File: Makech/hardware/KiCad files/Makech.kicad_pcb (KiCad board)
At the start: 2 copper layers, 54.9 x 88.5 mm, 50 parts, among them IC1 ULN2803, J1 SWD programmer, J2 USB_B_Micro, J3 ESP32-Exp, SW1 RST, SW2 SW_DPDT_x2, U1 ATSAMD21G18A-AU, U2 CONN_01X04, U3 AP2114_3.3v, X1 Screw_Terminal_1x02

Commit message: PCB COMPLETE
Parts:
- moved G*** 13.1 mm to (106.3, 90.9)
- moved SW1 1.24 mm to (128.5, 88.4)
- moved C2 0.79 mm to (132.6, 82.8)
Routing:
- net +3V3: track 31.9 -> 115.4 mm, vias 1 -> 6
- net Net-(R4-Pad2): track 12.5 -> 90.6 mm, vias 0 -> 2
- net /A1: track 0.00 -> 72.7 mm, vias 0 -> 6
- net /A2: track 0.00 -> 63.5 mm, vias 0 -> 6
- net Net-(SW1-Pad2): track 0.00 -> 63.5 mm, vias 0 -> 4
- net /SDA: track 0.00 -> 59.2 mm, vias 0 -> 1
- net /A0: track 0.00 -> 52.6 mm, vias 0 -> 6
- net /A6: track 2.54 -> 50.0 mm, vias 0 -> 4
- net Net-(R6-Pad2): track 12.5 -> 44.0 mm
- net +6V: track 76.4 -> 91.7 mm
- net Net-(F1-Pad1): track 17.5 -> 19.8 mm
- net /D7: track 35.4 -> 37.2 mm
- net /A3: track 45.0 -> 43.3 mm
- net /D4: track 17.3 -> 18.7 mm
- net /SCL: track 62.3 -> 61.0 mm
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
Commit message: v0.1
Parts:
- moved SW2 0.85 mm to (101.2, 89.1)
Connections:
- J3 pad 11: /ESP_RESET -> GND
- J3 pad 3: /ESP_CS -> +3V3
- U1 pad 23: /ESP_CS -> +3V3
- U1 pad 32: /ESP_RESET -> GND
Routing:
- net GND: track 4.54 -> 187.4 mm, vias 0 -> 16
- net +3V3: track 115.4 -> 199.8 mm, vias 6 -> 12
- net /ESP_RESET: track 35.4 -> 0.00 mm, vias 2 -> 0
- net /ESP_CS: track 11.5 -> 0.00 mm, vias 2 -> 0
- net +6V: track 91.7 -> 96.9 mm
- net /TX: track 26.1 -> 28.2 mm
- net /A2: track 63.5 -> 65.6 mm
- net Net-(D1-Pad1): track 43.1 -> 44.7 mm
- net /RX: track 32.4 -> 33.8 mm
- net /D11: track 42.9 -> 43.9 mm
- net /A3: track 43.3 -> 44.3 mm
- net /SDA: track 59.2 -> 60.0 mm
- net /D7: track 37.2 -> 38.0 mm
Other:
- net class source: trace_width 0.5 -> 0.3

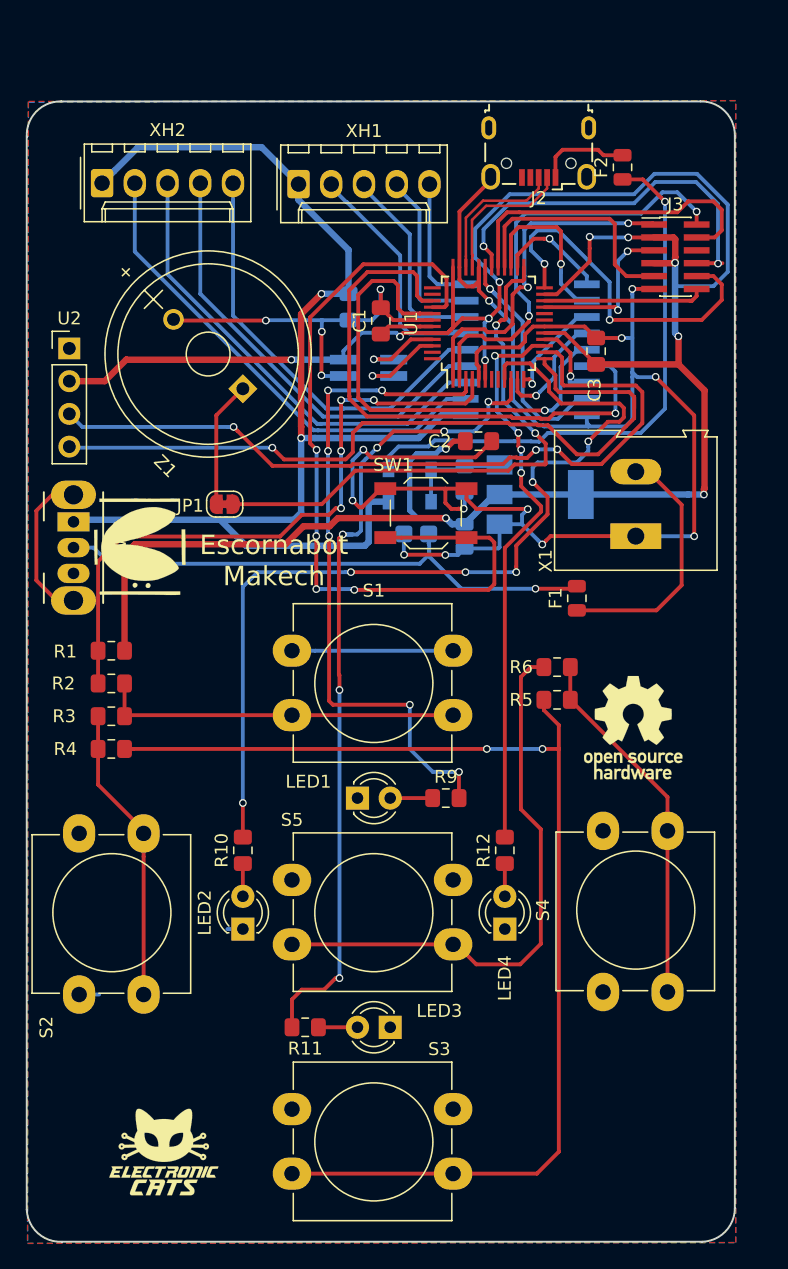
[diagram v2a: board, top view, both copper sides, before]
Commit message: update Silks
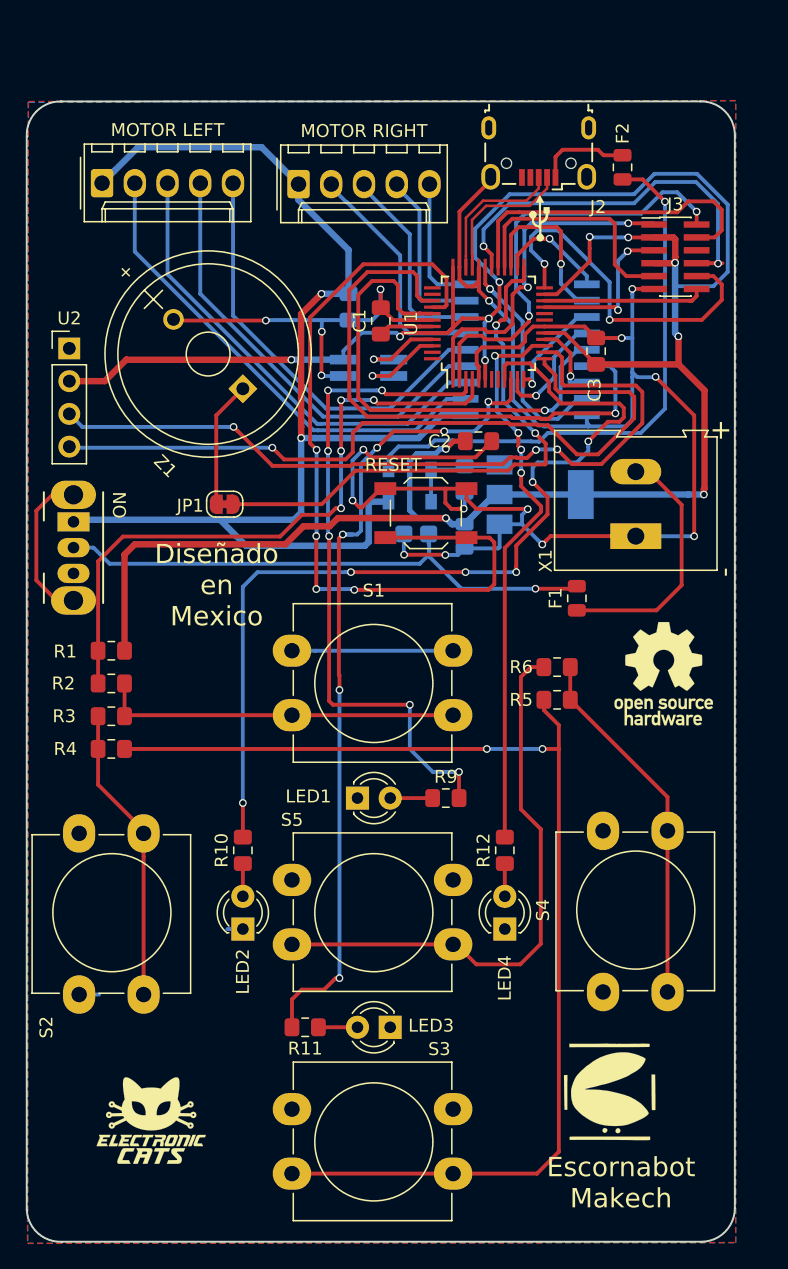
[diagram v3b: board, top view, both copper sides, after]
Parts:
- added G***: LOGO, Aesthetics:electronic_cats_logo_8x6, B.Cu at (140.8, 102.0)
- added svg2mod: G***, Aesthetics:usb_graphic, F.Cu at (137.3, 65.5)
- J1: value SWD programmer -> SWD
- MOTOR LEFT: renamed from XH2
- MOTOR RIGHT: renamed from XH1
- moved G*** 55.8 mm to (142.7, 133.2)
- moved G*** 5.90 mm to (143.3, 139.4)
- moved REF*** 4.81 mm to (146.9, 100.8)
- moved REF*** 4.07 mm to (109.2, 102.2)
- moved G*** 2.63 mm to (107.2, 135.5)
- moved REF*** 2.23 mm to (106.4, 136.7)
- renumbered SW2 to ON, SW1 to RESET
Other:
- board text added: "+"
- board text added: "-"
- board text added: "3V3"
- board text added: "Diseñado en Mexico"
- board text added: "GND"
- board text added: "SCL"
- board text added: "SDA"
- board text added: "electroniccats.com"

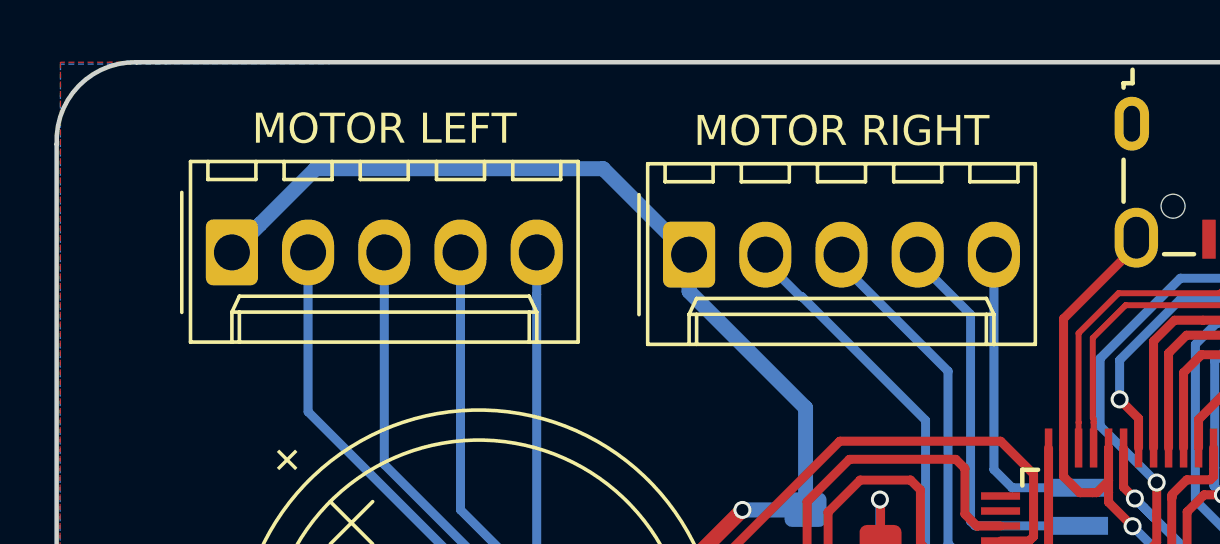
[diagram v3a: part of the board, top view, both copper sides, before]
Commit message: foot-print change
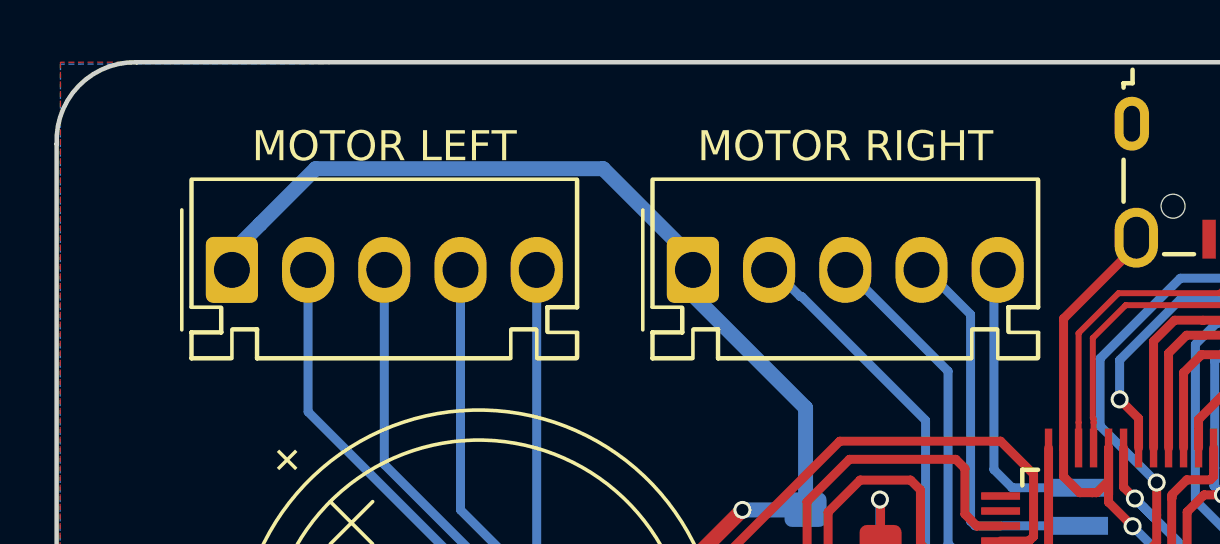
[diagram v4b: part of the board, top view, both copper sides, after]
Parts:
- removed the MOTOR LEFT at (103.4, 62.8)
- removed the MOTOR RIGHT at (118.6, 62.9)
- added MOTOR LEFT: CONN_01X05, ElectronicCats-KiCad-Libraries:Molex_KK-254_AE-6410-05A_1x05_P2.54mm_Vertical, F.Cu at (103.4, 63.4)
- added MOTOR RIGHT: CONN_01X05, ElectronicCats-KiCad-Libraries:Molex_KK-254_AE-6410-05A_1x05_P2.54mm_Vertical, F.Cu at (118.7, 63.4)
- J1: value SWD -> SWD programmer

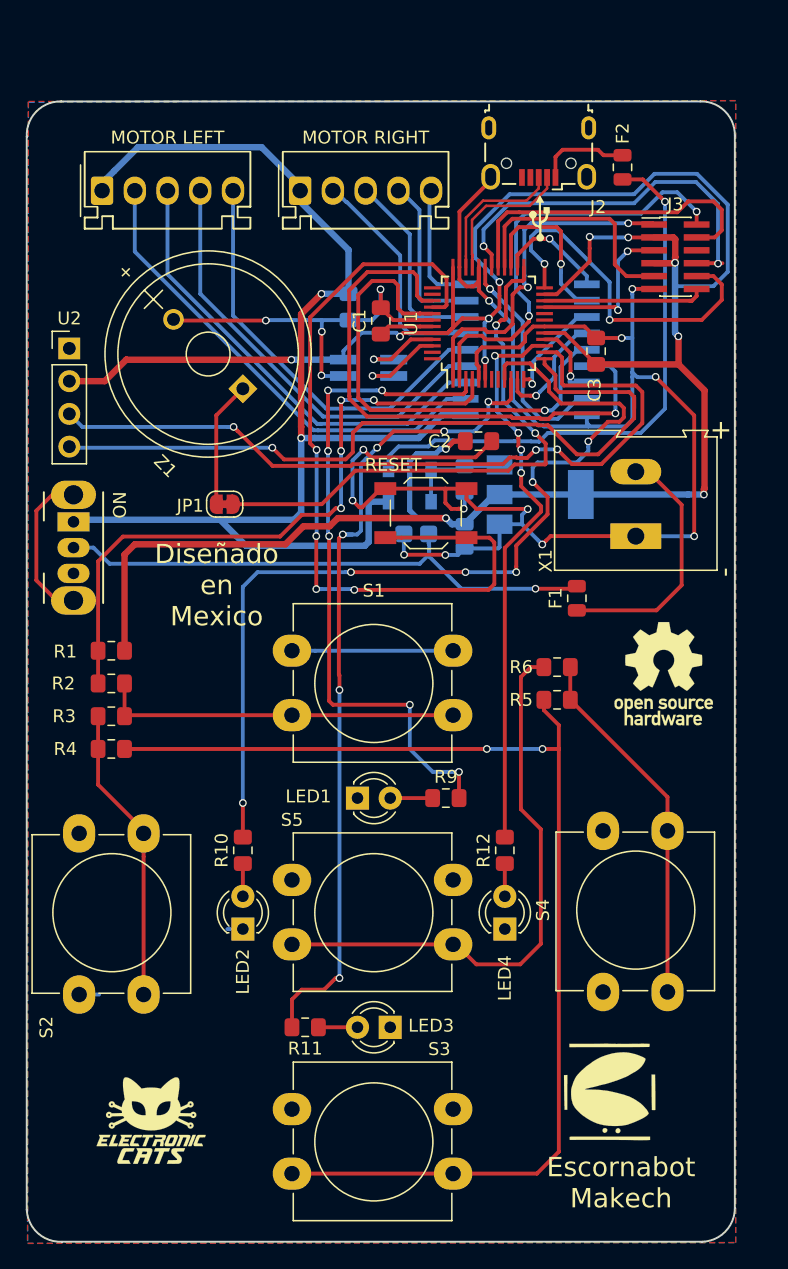
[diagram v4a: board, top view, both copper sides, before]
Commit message: Change connector ESP32, SWD and logo OSWHA
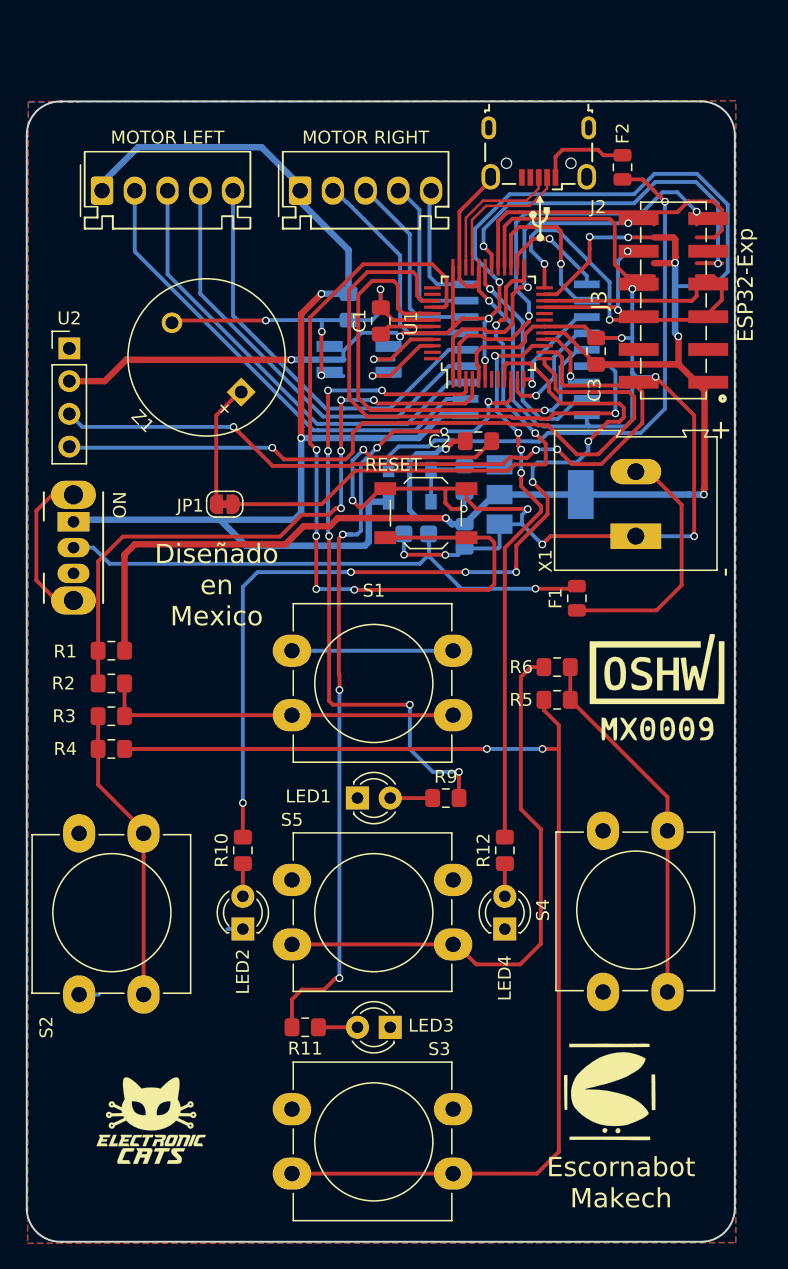
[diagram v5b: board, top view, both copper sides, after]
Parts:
- removed the REF*** at (146.9, 100.8)
- added G***: LOGO, Aesthetics:OSHW_MX0009, F.Cu at (146.4, 101.9)
- J1: footprint Pines:621X0421021 -> Pines:621X04245821
- J3: footprint Connector_PinHeader_1.00mm:PinHeader_2x06_P1.00mm_Vertical_SMD -> Pines:610X1221121
- Z1: footprint Buzzer_Beeper:MagneticBuzzer_StarMicronics_HMB-06_HMB-12 -> Buzzers_Beepers:MagneticBuzzer_ProSignal_ABI-009-RC
- moved J3 3.39 mm to (147.7, 71.9), turned to 90 degrees
- moved G*** 2.29 mm to (143.1, 102.1)
- moved REF*** 1.94 mm to (107.3, 102.6)
- moved J1 0.99 mm to (123.3, 76.5), turned to 270 degrees
- moved Z1 0.28 mm to (114.2, 79.0)
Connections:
- net /A6 renamed /A4
- IC1 pad 1: /D13 -> /D9
- IC1 pad 2: /D10 -> /D8
- IC1 pad 3: /D9 -> /D7
- IC1 pad 4: /D8 -> /D6
- IC1 pad 5: /D7 -> /D5
- IC1 pad 6: /D6 -> /D4
- IC1 pad 7: /D5 -> /D3
- IC1 pad 8: /D4 -> /D2
- JP1 pad 1: /D11 -> /D10
- U1 pad 11: /D8 -> /D6
- U1 pad 12: /D9 -> /D7
- U1 pad 16: /D5 -> /D3
- U1 pad 25: /D11 -> /D10
- U1 pad 26: /D13 -> /D9
- U1 pad 27: /D10 -> /D8
- U1 pad 31: /D4 -> /D2
- U1 pad 39: /D6 -> /D4
- U1 pad 41: /D7 -> /D5
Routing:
- net /D11: track 43.9 -> 0.00 mm, vias 2 -> 0
- net /D6: track 44.4 -> 9.40 mm
- net /D5: track 6.08 -> 38.0 mm
- net /D10: track 13.6 -> 43.9 mm, vias 1 -> 2
- net /D7: track 38.0 -> 8.24 mm
- net /D4: track 18.7 -> 44.4 mm
- net /D2: track 0.00 -> 18.7 mm, vias 0 -> 1
- net /D13: track 8.70 -> 0.00 mm, vias 1 -> 0
- net /D3: track 0.00 -> 6.08 mm, vias 0 -> 1
- net /D8: track 9.40 -> 13.6 mm

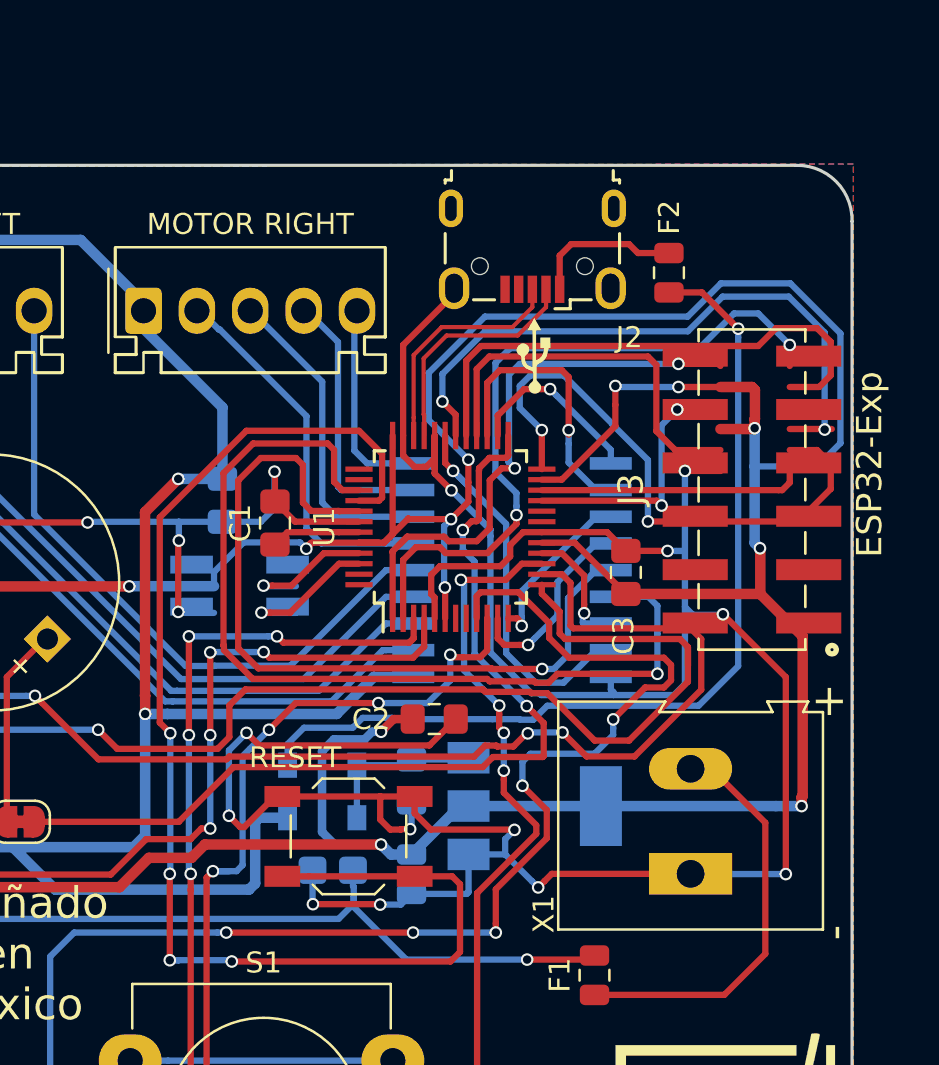
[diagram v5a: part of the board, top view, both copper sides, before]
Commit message: change terminal block
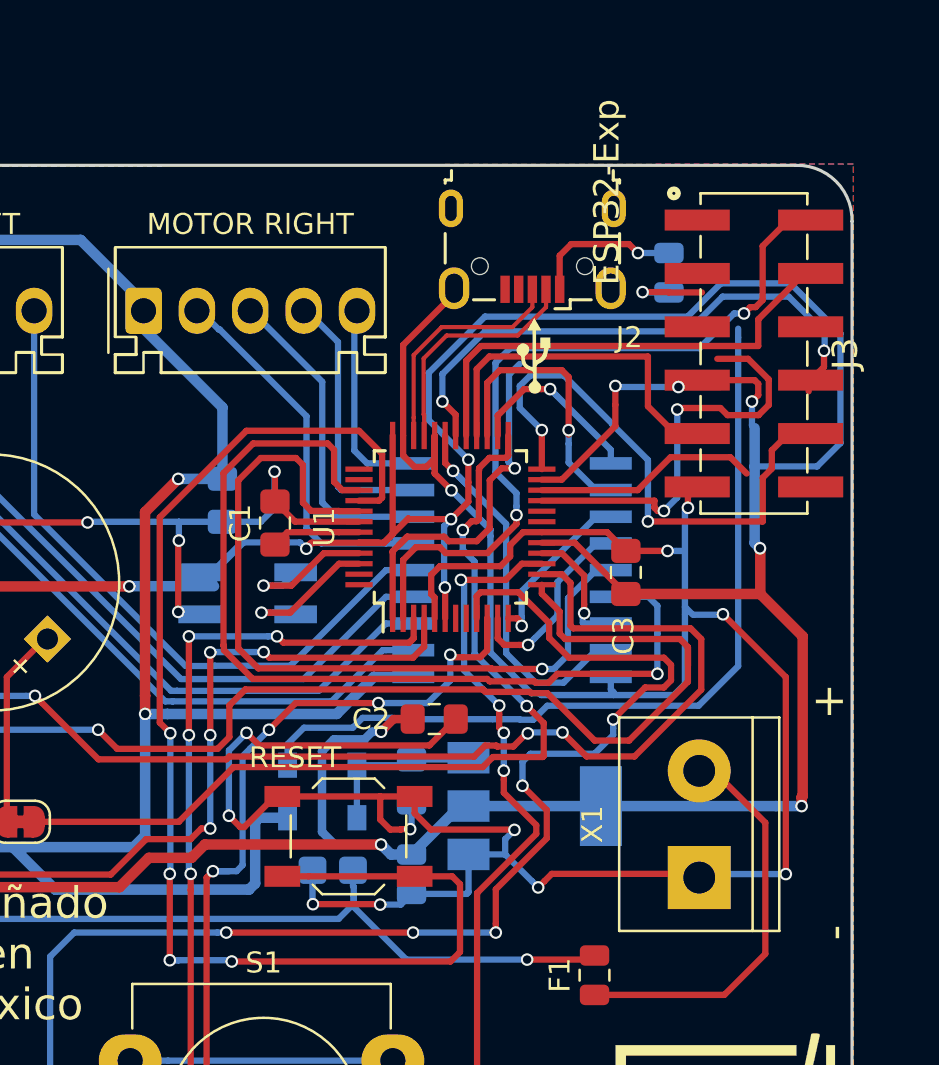
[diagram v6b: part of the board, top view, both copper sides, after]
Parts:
- F2: moved to B.Cu
- X1: footprint TerminalBlock:TerminalBlock_Altech_AK300-2_P5.00mm -> Terminal_Blocks:TerminalBlock_bornier-2_P5.08mm
- moved J3 6.48 mm to (147.8, 65.4), turned to 270 degrees
- moved J1 0.53 mm to (123.7, 76.8), turned to 90 degrees
- moved X1 0.45 mm to (145.2, 90.3)
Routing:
- net /TX: track 28.2 -> 18.6 mm, vias 2 -> 1
- net +3V3: track 199.8 -> 207.2 mm
- net /ESP_MOSI: track 12.8 -> 20.1 mm
- net /ESP_GPIO: track 25.6 -> 22.4 mm
- net /ESP_BUSY: track 30.2 -> 27.5 mm
- net /RX: track 33.8 -> 36.5 mm
- net /ESP_RTS: track 18.7 -> 16.8 mm
- net /ESP_MISO: track 12.5 -> 10.7 mm
- net /ESP_SCK: track 28.1 -> 26.5 mm
- net GND: track 187.4 -> 186.3 mm
- net Net-(F2-Pad2): vias 0 -> 1
